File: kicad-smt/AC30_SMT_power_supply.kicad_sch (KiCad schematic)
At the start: 15 parts, among them IC16 7805, P1 120 VAC line cord, T1 120/240V : 18VAC CT 300mA

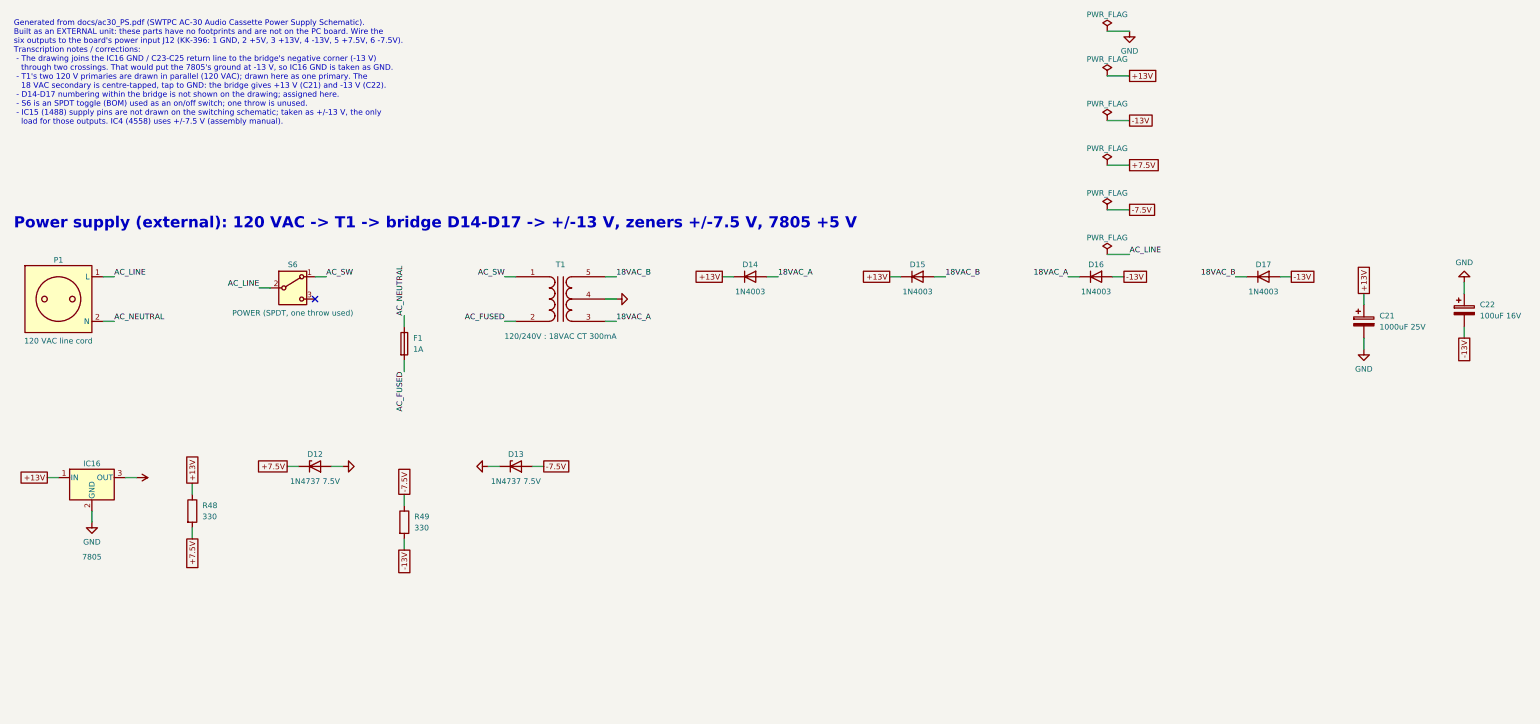
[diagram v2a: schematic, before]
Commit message: Wired, human-readable schematics with PDF and PNG images
gen.py now lays out each functional group on its own and draws its nets
as real wires (new tools/schroute.py: orthogonal grid router that never
ends, bends or overlaps on another net's wire); every routed net keeps
one label with its name, labels join nets between blocks and sheets, and
unroutable connections fall back to label pairs (17). The front-panel
jumper pads share the front-panel block. Custom 1488/1489 output pins
moved onto the 2.54 mm grid.

build.sh exports schematic/<project>.pdf and, via tools/schimg.py, PNGs
of every sheet and functional block for both boards.

Connectivity unchanged (pin-to-net maps identical for both variants);
ERC 0; both PCBs DRC/parity clean and unchanged. Docs updated.

Co-Authored-By: Claude Opus 5.5 <noreply@anthropic.com>
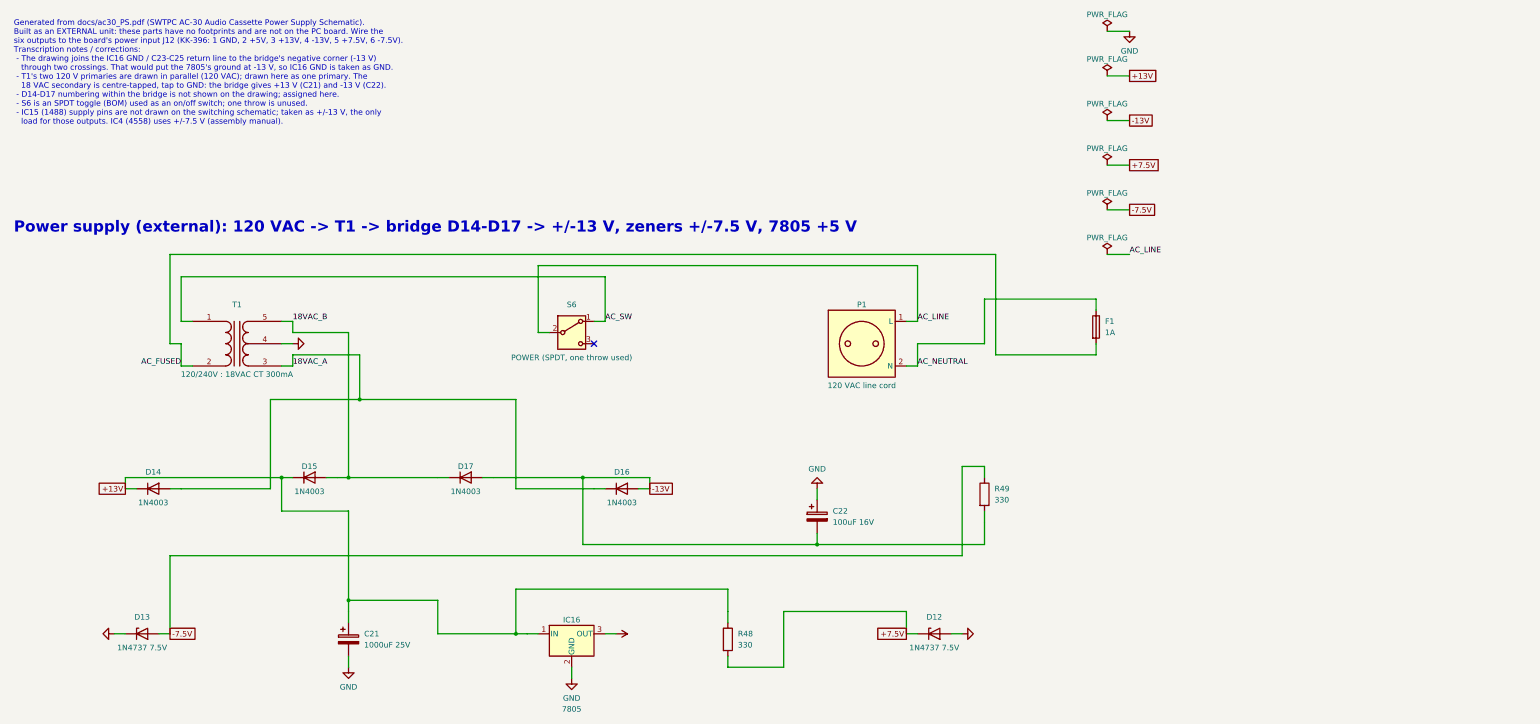
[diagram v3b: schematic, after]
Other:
- moved on the sheet: C21, C22, D12, D13, D14, D15, D16, D17, F1, IC16, P1, R48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
